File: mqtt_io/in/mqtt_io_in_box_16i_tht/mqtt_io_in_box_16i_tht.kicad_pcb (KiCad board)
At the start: 2 copper layers, 140.2 x 120.6 mm, 94 parts, among them J1 Conn_01x04_Pin, J2 Conn_01x04_Pin, U1 MCP23017_SP, U10 LTV-817, U11 LTV-817, U12 LTV-817, U13 LTV-817, U14 LTV-817, U15 LTV-817, U16 LTV-817, U17 LTV-817, U2 LTV-817, U3 LTV-817, U4 LTV-817, U5 LTV-817, U6 LTV-817, U7 LTV-817, U8 LTV-817, U9 LTV-817

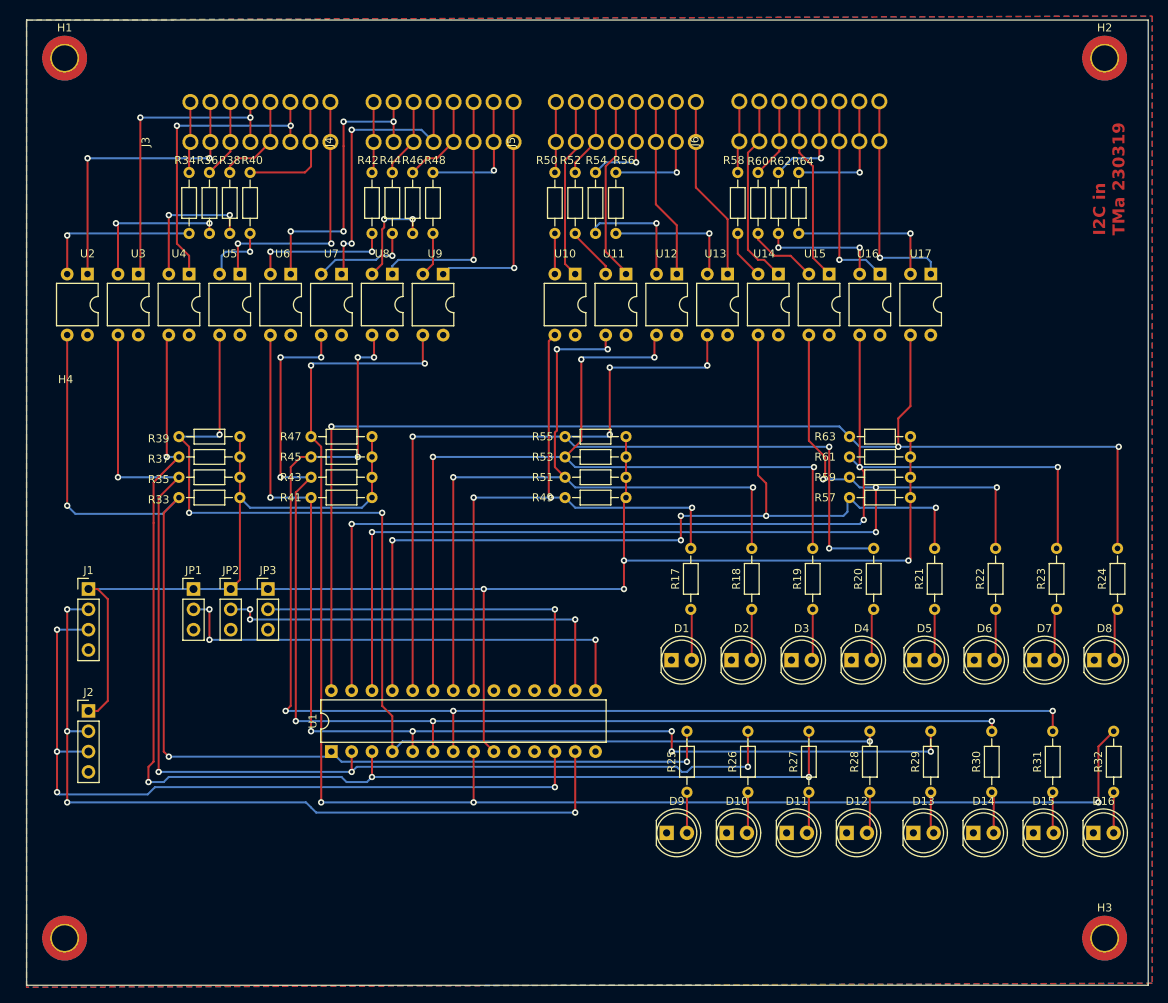
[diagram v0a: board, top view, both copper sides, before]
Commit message: Pullup für ic2 eingefügt (4k7)
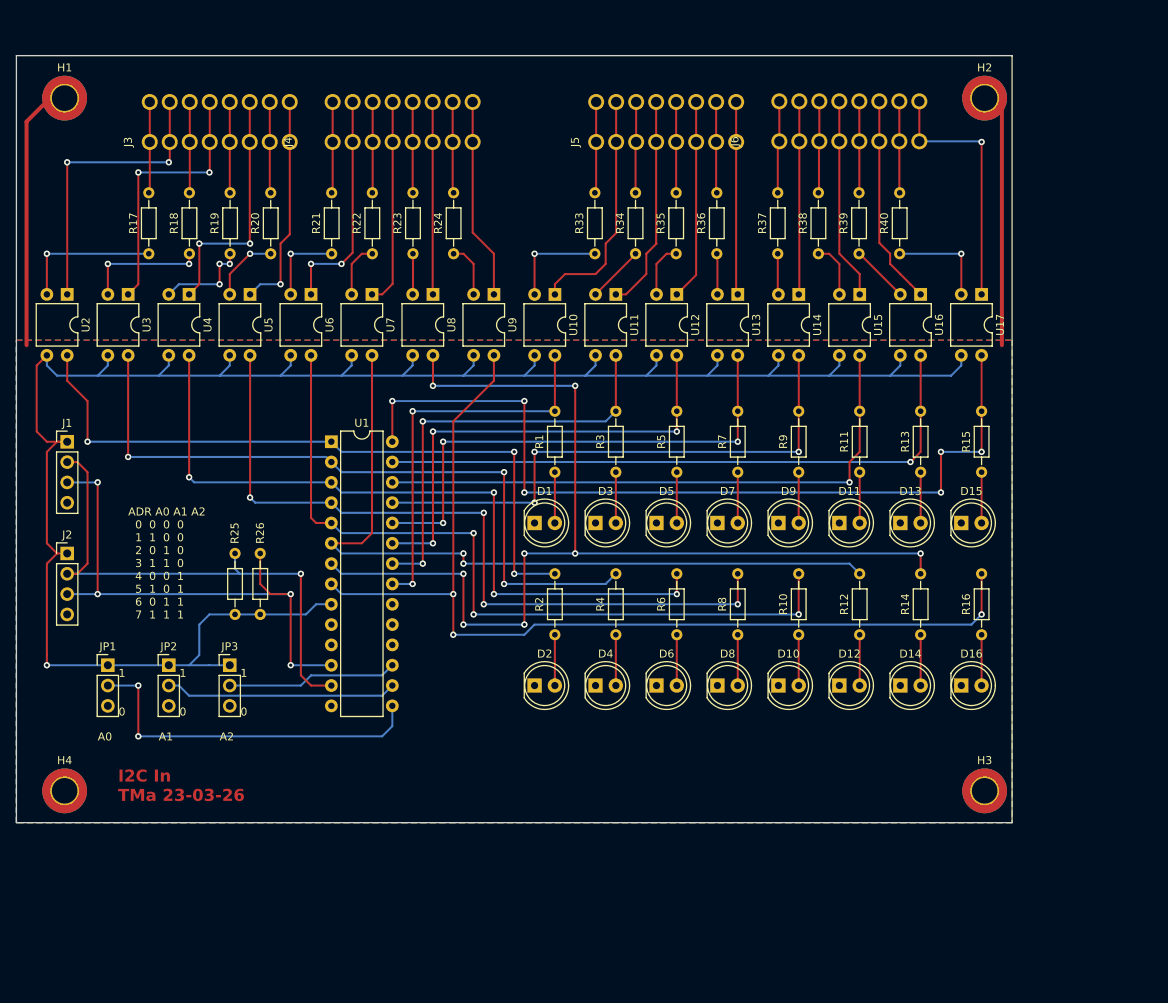
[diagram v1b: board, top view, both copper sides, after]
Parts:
- removed R27, R28, R29, R30, R31, R32: 330R, Resistor_THT:R_Axial_DIN0204_L3.6mm_D1.6mm_P7.62mm_Horizontal
- removed R41, R43, R45, R47, R49, R51, R53, R55, R57, R59, R61, R63: 10kR, Resistor_THT:R_Axial_DIN0204_L3.6mm_D1.6mm_P7.62mm_Horizontal
- removed R42, R44, R46, R48, R50, R52, R54, R56, R58, R60, R62, R64: 1200R, Resistor_THT:R_Axial_DIN0204_L3.6mm_D1.6mm_P7.62mm_Horizontal
- added R1: 330R, Resistor_THT:R_Axial_DIN0204_L3.6mm_D1.6mm_P7.62mm_Horizontal, F.Cu at (81.3, 71.8)
- added R10: 330R, Resistor_THT:R_Axial_DIN0204_L3.6mm_D1.6mm_P7.62mm_Horizontal, F.Cu at (111.8, 92.1)
- added R11: 330R, Resistor_THT:R_Axial_DIN0204_L3.6mm_D1.6mm_P7.62mm_Horizontal, F.Cu at (119.4, 71.8)
- added R12: 330R, Resistor_THT:R_Axial_DIN0204_L3.6mm_D1.6mm_P7.62mm_Horizontal, F.Cu at (119.4, 92.1)
- added R13: 330R, Resistor_THT:R_Axial_DIN0204_L3.6mm_D1.6mm_P7.62mm_Horizontal, F.Cu at (127.0, 71.8)
- added R14: 330R, Resistor_THT:R_Axial_DIN0204_L3.6mm_D1.6mm_P7.62mm_Horizontal, F.Cu at (127.0, 92.1)
- added R15: 330R, Resistor_THT:R_Axial_DIN0204_L3.6mm_D1.6mm_P7.62mm_Horizontal, F.Cu at (134.6, 71.8)
- added R16: 330R, Resistor_THT:R_Axial_DIN0204_L3.6mm_D1.6mm_P7.62mm_Horizontal, F.Cu at (134.6, 92.1)
- added R2: 330R, Resistor_THT:R_Axial_DIN0204_L3.6mm_D1.6mm_P7.62mm_Horizontal, F.Cu at (81.3, 92.1)
- added R3: 330R, Resistor_THT:R_Axial_DIN0204_L3.6mm_D1.6mm_P7.62mm_Horizontal, F.Cu at (88.9, 71.8)
- added R4: 330R, Resistor_THT:R_Axial_DIN0204_L3.6mm_D1.6mm_P7.62mm_Horizontal, F.Cu at (88.9, 92.1)
- added R5: 330R, Resistor_THT:R_Axial_DIN0204_L3.6mm_D1.6mm_P7.62mm_Horizontal, F.Cu at (96.5, 71.8)
- added R6: 330R, Resistor_THT:R_Axial_DIN0204_L3.6mm_D1.6mm_P7.62mm_Horizontal, F.Cu at (96.5, 92.1)
- added R7: 330R, Resistor_THT:R_Axial_DIN0204_L3.6mm_D1.6mm_P7.62mm_Horizontal, F.Cu at (104.1, 71.8)
- added R8: 330R, Resistor_THT:R_Axial_DIN0204_L3.6mm_D1.6mm_P7.62mm_Horizontal, F.Cu at (104.1, 92.1)
- added R9: 330R, Resistor_THT:R_Axial_DIN0204_L3.6mm_D1.6mm_P7.62mm_Horizontal, F.Cu at (111.8, 71.8)
- R17, R18, R19, R20, R21, R22, R23, R24: value 330R -> 1200R
- R25, R26: value 330R -> 4k7
- R33, R35, R37, R39: value 10kR -> 1200R
- moved R24 94.1 mm to (68.6, 44.5)
- moved R23 91.9 mm to (63.5, 44.5)
- moved R22 89.7 mm to (58.5, 44.5)
- moved R20 87.5 mm to (45.8, 44.5)
- moved R21 87.5 mm to (53.4, 44.5)
- moved R19 85.3 mm to (40.7, 44.5)
- moved R18 83.2 mm to (35.6, 44.5)
- moved R40 81.2 mm to (124.4, 44.5)
- moved R17 81.0 mm to (30.5, 44.5)
- moved R39 80.7 mm to (119.3, 44.5), turned to 90 degrees
- moved R38 73.6 mm to (114.2, 44.5)
- moved R37 71.9 mm to (109.1, 44.5), turned to 90 degrees
- moved R26 64.9 mm to (44.5, 89.5)
- moved R36 63.5 mm to (101.5, 44.5)
- moved R35 61.3 mm to (96.4, 44.5), turned to 90 degrees
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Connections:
- R17 pad 1: Net-(D1-A) -> Net-(R17-Pad1)
- R17 pad 2: /a0 -> Net-(J3-io-Pad1)
- R18 pad 1: Net-(D2-A) -> Net-(R18-Pad1)
- R18 pad 2: /a1 -> Net-(J3-io-Pad3)
- R19 pad 1: Net-(D3-A) -> Net-(R19-Pad1)
- R19 pad 2: /a2 -> Net-(J3-io-Pad5)
- R20 pad 1: Net-(D4-A) -> Net-(R20-Pad1)
- R20 pad 2: /a3 -> Net-(J3-io-Pad7)
- R21 pad 1: Net-(D5-A) -> Net-(R21-Pad1)
- R21 pad 2: /a4 -> Net-(J4-io-Pad1)
- R22 pad 1: Net-(D6-A) -> Net-(R22-Pad1)
- R22 pad 2: /a5 -> Net-(J4-io-Pad3)
- R23 pad 1: Net-(D7-A) -> Net-(R23-Pad1)
- R23 pad 2: /a6 -> Net-(J4-io-Pad5)
- R24 pad 1: Net-(D8-A) -> Net-(R24-Pad1)
- R24 pad 2: /a7 -> Net-(J4-io-Pad7)
- R25 pad 1: Net-(D9-A) -> +5V
- R25 pad 2: /b0 -> Net-(J1-Pin_2)
- R26 pad 1: Net-(D10-A) -> +5V
- R26 pad 2: /b1 -> Net-(J1-Pin_3)
- R33 pad 1: +5V -> Net-(R33-Pad1)
- R33 pad 2: /b0 -> Net-(J5-io-Pad1)
- R34 pad 2: Net-(J3-io-Pad1) -> Net-(J5-io-Pad3)
- R35 pad 1: +5V -> Net-(R35-Pad1)
- R35 pad 2: /b1 -> Net-(J5-io-Pad5)
- R36 pad 2: Net-(J3-io-Pad3) -> Net-(J5-io-Pad7)
- R37 pad 1: +5V -> Net-(R37-Pad1)
- R37 pad 2: /b2 -> Net-(J6-io-Pad1)
- R38 pad 2: Net-(J3-io-Pad5) -> Net-(J6-io-Pad3)
- R39 pad 1: +5V -> Net-(R39-Pad1)
- R39 pad 2: /b3 -> Net-(J6-io-Pad5)
- R40 pad 2: Net-(J3-io-Pad7) -> Net-(J6-io-Pad7)
- U10 pad 2: Net-(R50-Pad1) -> Net-(R33-Pad1)
- U10 pad 3: /a0 -> +5V
- U10 pad 4: GND -> /a0
- U11 pad 2: Net-(R52-Pad1) -> Net-(R34-Pad1)
- U11 pad 3: /a1 -> +5V
- U11 pad 4: GND -> /a1
- U12 pad 2: Net-(R54-Pad1) -> Net-(R35-Pad1)
- U12 pad 3: /a2 -> +5V
- U12 pad 4: GND -> /a2
- U13 pad 2: Net-(R56-Pad1) -> Net-(R36-Pad1)
- U13 pad 3: /a3 -> +5V
- U13 pad 4: GND -> /a3
- U14 pad 2: Net-(R58-Pad1) -> Net-(R37-Pad1)
- U14 pad 3: /a4 -> +5V
- U14 pad 4: GND -> /a4
- U15 pad 2: Net-(R60-Pad1) -> Net-(R38-Pad1)
- U15 pad 3: /a5 -> +5V
- U15 pad 4: GND -> /a5
- U16 pad 2: Net-(R62-Pad1) -> Net-(R39-Pad1)
- U16 pad 3: /a6 -> +5V
- U16 pad 4: GND -> /a6
- U17 pad 2: Net-(R64-Pad1) -> Net-(R40-Pad1)
- U17 pad 3: /a7 -> +5V
- U17 pad 4: GND -> /a7
- U2 pad 2: Net-(R34-Pad1) -> Net-(R17-Pad1)
- U2 pad 3: /b0 -> +5V
- U2 pad 4: GND -> /b0
- U3 pad 2: Net-(R36-Pad1) -> Net-(R18-Pad1)
- U3 pad 3: /b1 -> +5V
- U3 pad 4: GND -> /b1
- U4 pad 2: Net-(R38-Pad1) -> Net-(R19-Pad1)
- U4 pad 3: /b2 -> +5V
- U4 pad 4: GND -> /b2
- U5 pad 2: Net-(R40-Pad1) -> Net-(R20-Pad1)
- U5 pad 3: /b3 -> +5V
- U5 pad 4: GND -> /b3
- U6 pad 2: Net-(R42-Pad1) -> Net-(R21-Pad1)
- U6 pad 3: /b4 -> +5V
- U6 pad 4: GND -> /b4
- U7 pad 2: Net-(R44-Pad1) -> Net-(R22-Pad1)
- U7 pad 3: /b5 -> +5V
- U7 pad 4: GND -> /b5
- U8 pad 2: Net-(R46-Pad1) -> Net-(R23-Pad1)
- U8 pad 3: /b6 -> +5V
- U8 pad 4: GND -> /b6
- U9 pad 2: Net-(R48-Pad1) -> Net-(R24-Pad1)
- U9 pad 3: /b7 -> +5V
- U9 pad 4: GND -> /b7
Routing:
- net /a3: track 132.8 -> 64.1 mm, vias 6 -> 3
- net GND: track 0.00 -> 66.7 mm
- net /a6: track 145.2 -> 78.6 mm, vias 4 -> 1
- net /a5: track 137.4 -> 73.5 mm, vias 5 -> 1
- net /b7: track 186.3 -> 125.0 mm, vias 5 -> 3
- net /b2: track 151.3 -> 92.2 mm
- net /b1: track 144.7 -> 88.9 mm, vias 4 -> 3
- net /b5: track 150.0 -> 96.2 mm, vias 6 -> 2
- net /a2: track 112.8 -> 59.1 mm, vias 4 -> 3
- net /b0: track 139.4 -> 86.0 mm
- net /a7: track 159.9 -> 107.3 mm, vias 3 -> 6
- net /a4: track 120.3 -> 69.2 mm, vias 5 -> 3
- net /b3: track 143.7 -> 94.8 mm
- net /a1: track 97.2 -> 53.2 mm, vias 4 -> 2
- net /b4: track 139.7 -> 97.3 mm, vias 6 -> 3
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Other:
- board size 140.2 x 120.6 mm -> 124.5 x 95.9 mm
- board text added: "1 0"
- board text added: "A0"
- board text added: "A1"
- board text added: "A2"
- board text added: "ADR A0 A1 A2 0 0 0 0 1 1 0 0 2 0 1 0 3 1 1 0 4 0 0 1 5 1 0 1 6 0 1 1 7 1 1 1"
- board text added: "I2C In TMa 23-03-26"
- board text removed: "I2C in TMa 230319"

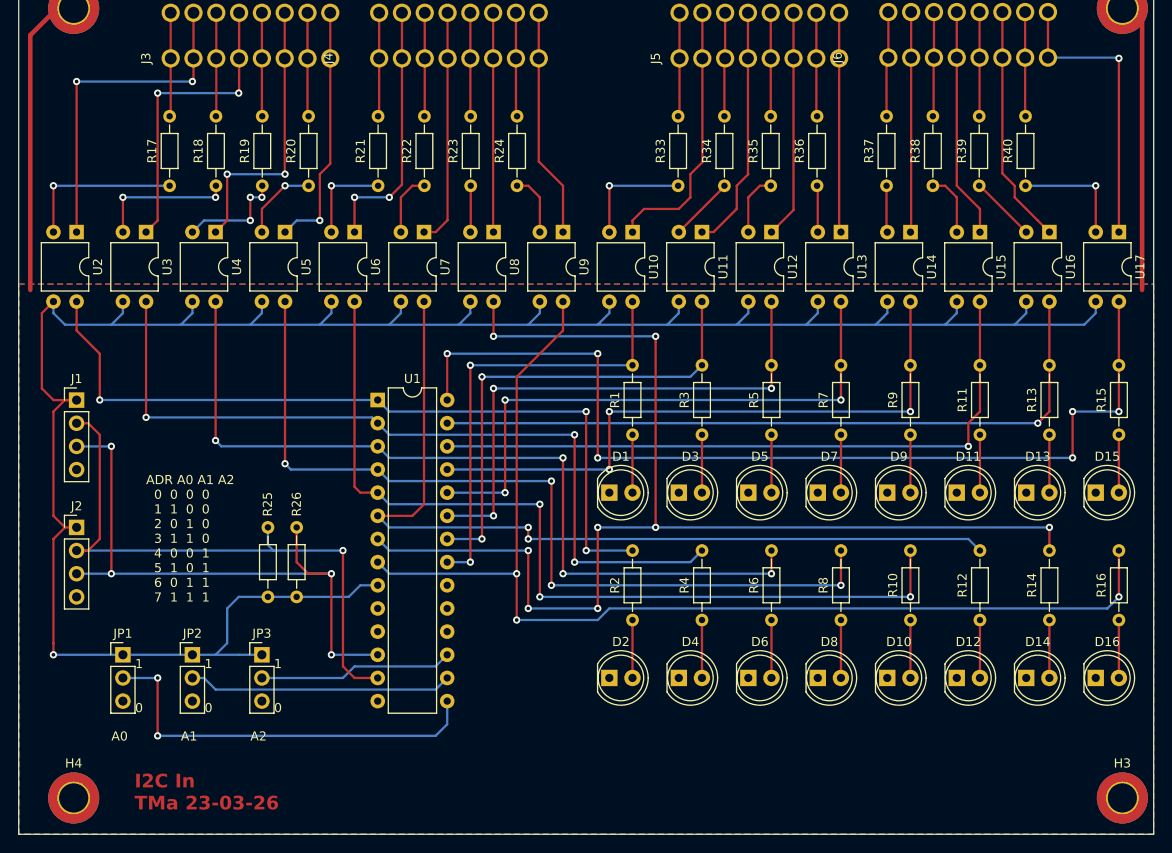
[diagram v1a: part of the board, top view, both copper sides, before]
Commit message: neue Dateien eingefügt.
out Platine rev 2, testprogramm für pi pico
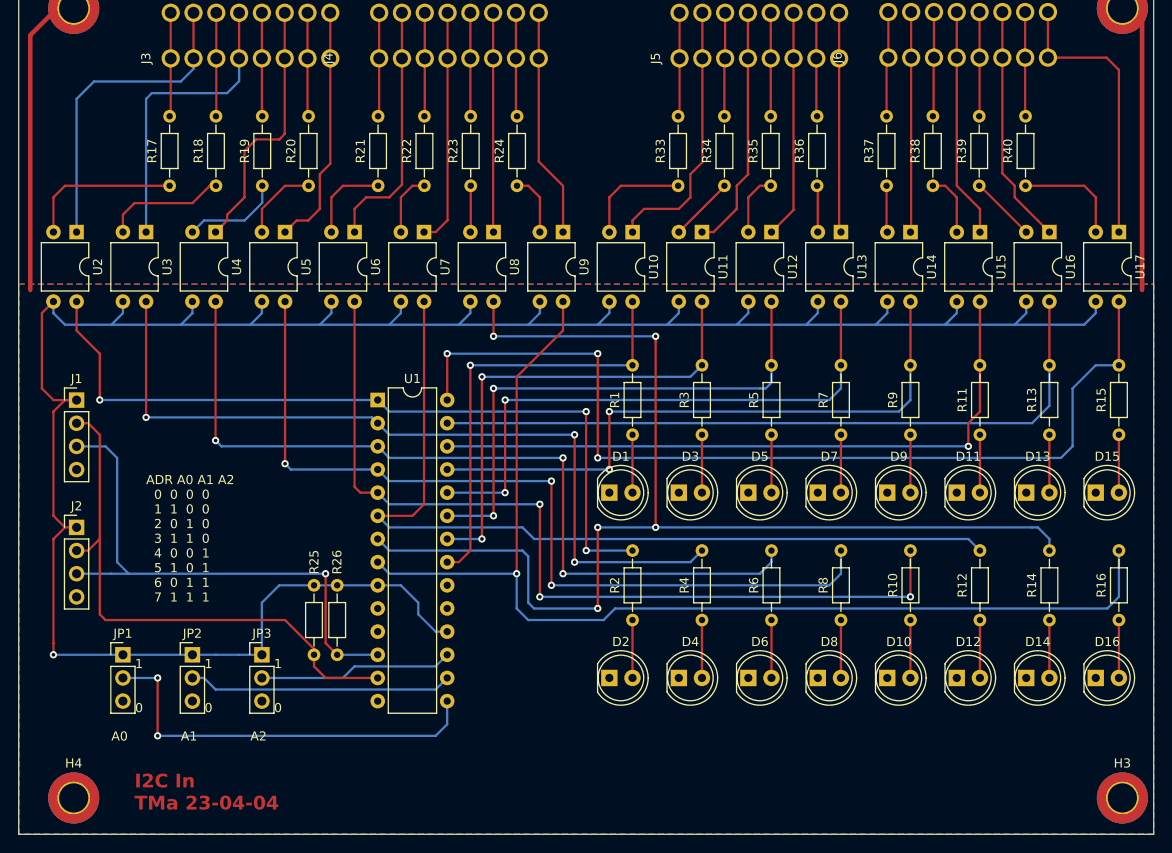
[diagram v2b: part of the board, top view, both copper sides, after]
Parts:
- moved R25 5.21 mm to (46.4, 88.3), turned to -90 degrees
- moved R26 4.62 mm to (48.9, 88.3), turned to -90 degrees
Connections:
- J1 pad 1: +5V -> VDD
- J2 pad 1: +5V -> VDD
- JP1 pad 1: +5V -> VDD
- JP2 pad 1: +5V -> VDD
- JP3 pad 1: +5V -> VDD
- R25 pad 1: +5V -> VDD
- R26 pad 1: +5V -> VDD
- U1 pad 18: GND -> VDD
- U1 pad 9: +5V -> VDD
- U10 pad 3: +5V -> VDD
- U11 pad 3: +5V -> VDD
- U12 pad 3: +5V -> VDD
- U13 pad 3: +5V -> VDD
- U14 pad 3: +5V -> VDD
- U15 pad 3: +5V -> VDD
- U16 pad 3: +5V -> VDD
- U17 pad 3: +5V -> VDD
- U2 pad 3: +5V -> VDD
- U3 pad 3: +5V -> VDD
- U4 pad 3: +5V -> VDD
- U5 pad 3: +5V -> VDD
- U6 pad 3: +5V -> VDD
- U7 pad 3: +5V -> VDD
- U8 pad 3: +5V -> VDD
- U9 pad 3: +5V -> VDD
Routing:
- net VDD: track 0.00 -> 259.8 mm, vias 0 -> 1
- net +5V: track 253.3 -> 0.00 mm, vias 1 -> 0
- net Net-(J1-Pin_3): track 67.8 -> 59.4 mm, vias 4 -> 1
- net Net-(J1-Pin_2): track 66.6 -> 60.3 mm, vias 1 -> 0
- net Net-(J3-io-Pad6): track 30.9 -> 28.7 mm, vias 2 -> 0
- net /a7: track 107.3 -> 105.1 mm, vias 6 -> 3
- net Net-(J3-io-Pad2): track 36.8 -> 34.9 mm, vias 2 -> 0
- net Net-(R18-Pad1): track 15.3 -> 13.4 mm, vias 2 -> 0
- net /b6: track 134.5 -> 133.0 mm, vias 8 -> 5
- net Net-(R19-Pad1): track 12.0 -> 10.9 mm, vias 3 -> 0
- net /b7: track 125.0 -> 124.2 mm, vias 3 -> 1
- net /b2: track 92.2 -> 91.5 mm, vias 4 -> 3
- net /a4: track 69.2 -> 68.5 mm, vias 3 -> 2
- net Net-(J4-io-Pad2): track 28.4 -> 27.7 mm, vias 2 -> 0
- net /a0: track 48.9 -> 48.1 mm, vias 2 -> 1
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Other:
- board text added: "I2C In TMa 23-04-04"
- board text removed: "I2C In TMa 23-03-26"

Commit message: Add files via upload
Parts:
- removed JP1, JP2, JP3: Jumper_3_Open, Connector_PinHeader_2.54mm:PinHeader_1x03_P2.54mm_Vertical
- added D17: 5,1V, Diode_THT:D_DO-41_SOD81_P10.16mm_Horizontal, F.Cu at (-85.7, 53.7)
- added D18: 5,1V, Diode_THT:D_DO-41_SOD81_P10.16mm_Horizontal, F.Cu at (-85.7, 58.0)
- added D19: 5,1V, Diode_THT:D_DO-41_SOD81_P10.16mm_Horizontal, F.Cu at (-85.7, 62.2)
- added D20: 5,1V, Diode_THT:D_DO-41_SOD81_P10.16mm_Horizontal, F.Cu at (-85.7, 66.5)
- added D21: 5,1V, Diode_THT:D_DO-41_SOD81_P10.16mm_Horizontal, F.Cu at (-85.7, 70.7)
- added D22: 5,1V, Diode_THT:D_DO-41_SOD81_P10.16mm_Horizontal, F.Cu at (-85.7, 75.0)
- added D23: 5,1V, Diode_THT:D_DO-41_SOD81_P10.16mm_Horizontal, F.Cu at (-85.7, 79.2)
- added D24: 5,1V, Diode_THT:D_DO-41_SOD81_P10.16mm_Horizontal, F.Cu at (-85.7, 83.5)
- added D25: LED, Diode_THT:D_DO-41_SOD81_P10.16mm_Horizontal, F.Cu at (-85.7, 87.7)
- added D26: LED, Diode_THT:D_DO-41_SOD81_P10.16mm_Horizontal, F.Cu at (-85.7, 92.0)
- added D27: LED, Diode_THT:D_DO-41_SOD81_P10.16mm_Horizontal, F.Cu at (-85.7, 96.2)
- added D28: LED, Diode_THT:D_DO-41_SOD81_P10.16mm_Horizontal, F.Cu at (-85.7, 100.5)
- added D29: LED, Diode_THT:D_DO-41_SOD81_P10.16mm_Horizontal, F.Cu at (-85.7, 104.7)
- added D30: LED, Diode_THT:D_DO-41_SOD81_P10.16mm_Horizontal, F.Cu at (-85.7, 109.0)
- added D31: LED, Diode_THT:D_DO-41_SOD81_P10.16mm_Horizontal, F.Cu at (-85.7, 113.2)
- added D32: LED, Diode_THT:D_DO-41_SOD81_P10.16mm_Horizontal, F.Cu at (-85.7, 117.5)
- added J10: Sig_in_1, parts_tma_1:AST_041-2, F.Cu at (66.7, 33.7)
- added J11: Sig_in_1, parts_tma_1:AST_041-2, F.Cu at (73.0, 33.7)
- added J12: Sig_in_1, parts_tma_1:AST_041-2, F.Cu at (79.4, 33.7)
- added J13: Sig_in_1, parts_tma_1:AST_041-2, F.Cu at (85.7, 33.7)
- added J14: Sig_in_1, parts_tma_1:AST_041-2, F.Cu at (92.1, 33.7)
- added J15: Sig_in_1, parts_tma_1:AST_041-2, F.Cu at (98.4, 33.7)
- added J16: Sig_in_1, parts_tma_1:AST_041-2, F.Cu at (104.8, 33.7)
- added J17: Sig_in_1, parts_tma_1:AST_041-2, F.Cu at (111.1, 33.7)
- added J18: Sig_in_1, parts_tma_1:AST_041-2, F.Cu at (117.5, 33.7)
- added J19: Sig_in_1, parts_tma_1:AST_041-2, F.Cu at (123.8, 33.7)
- added J7: Sig_in_1, parts_tma_1:AST_041-2, F.Cu at (47.6, 33.7)
- added J8: Sig_in_1, parts_tma_1:AST_041-2, F.Cu at (54.0, 33.7)
- added J9: Sig_in_1, parts_tma_1:AST_041-2, F.Cu at (60.3, 33.7)
- added R27: 82R, Resistor_THT:R_Axial_DIN0204_L3.6mm_D1.6mm_P7.62mm_Horizontal, F.Cu at (-72.2, 53.2)
- added R28: 82R, Resistor_THT:R_Axial_DIN0204_L3.6mm_D1.6mm_P7.62mm_Horizontal, F.Cu at (-72.2, 56.3)
- added R29: 10k, Resistor_THT:R_Axial_DIN0204_L3.6mm_D1.6mm_P7.62mm_Horizontal, F.Cu at (-72.2, 59.5)
- added R30: 10k, Resistor_THT:R_Axial_DIN0204_L3.6mm_D1.6mm_P7.62mm_Horizontal, F.Cu at (-72.2, 62.6)
- added R31: 10k, Resistor_THT:R_Axial_DIN0204_L3.6mm_D1.6mm_P7.62mm_Horizontal, F.Cu at (-72.2, 65.8)
- added R32: 10k, Resistor_THT:R_Axial_DIN0204_L3.6mm_D1.6mm_P7.62mm_Horizontal, F.Cu at (-72.2, 68.9)
- added R41: R, Resistor_THT:R_Axial_DIN0204_L3.6mm_D1.6mm_P7.62mm_Horizontal, F.Cu at (-72.2, 72.1)
- added R42: R, Resistor_THT:R_Axial_DIN0204_L3.6mm_D1.6mm_P7.62mm_Horizontal, F.Cu at (-72.2, 75.2)
- added R43: R, Resistor_THT:R_Axial_DIN0204_L3.6mm_D1.6mm_P7.62mm_Horizontal, F.Cu at (-72.2, 78.4)
- added R44: R, Resistor_THT:R_Axial_DIN0204_L3.6mm_D1.6mm_P7.62mm_Horizontal, F.Cu at (-72.2, 81.5)
- added R45: 680R, Resistor_THT:R_Axial_DIN0204_L3.6mm_D1.6mm_P7.62mm_Horizontal, F.Cu at (-72.2, 84.7)
- added R46: 680R, Resistor_THT:R_Axial_DIN0204_L3.6mm_D1.6mm_P7.62mm_Horizontal, F.Cu at (-72.2, 87.8)
- added R47: 680R, Resistor_THT:R_Axial_DIN0204_L3.6mm_D1.6mm_P7.62mm_Horizontal, F.Cu at (-61.6, 53.2)
- added R48: 680R, Resistor_THT:R_Axial_DIN0204_L3.6mm_D1.6mm_P7.62mm_Horizontal, F.Cu at (-61.6, 56.3)
- added R49: 680R, Resistor_THT:R_Axial_DIN0204_L3.6mm_D1.6mm_P7.62mm_Horizontal, F.Cu at (-61.6, 59.5)
- added R50: 680R, Resistor_THT:R_Axial_DIN0204_L3.6mm_D1.6mm_P7.62mm_Horizontal, F.Cu at (-61.6, 62.6)
- added R51: 680R, Resistor_THT:R_Axial_DIN0204_L3.6mm_D1.6mm_P7.62mm_Horizontal, F.Cu at (-61.6, 65.8)
- added R52: 680R, Resistor_THT:R_Axial_DIN0204_L3.6mm_D1.6mm_P7.62mm_Horizontal, F.Cu at (-61.6, 68.9)
- added R53: 82R, Resistor_THT:R_Axial_DIN0204_L3.6mm_D1.6mm_P7.62mm_Horizontal, F.Cu at (-61.6, 72.1)
- added R54: 82R, Resistor_THT:R_Axial_DIN0204_L3.6mm_D1.6mm_P7.62mm_Horizontal, F.Cu at (-61.6, 75.2)
- added R55: 82R, Resistor_THT:R_Axial_DIN0204_L3.6mm_D1.6mm_P7.62mm_Horizontal, F.Cu at (-61.6, 78.4)
- added R56: 82R, Resistor_THT:R_Axial_DIN0204_L3.6mm_D1.6mm_P7.62mm_Horizontal, F.Cu at (-61.6, 81.5)
- added R57: 82R, Resistor_THT:R_Axial_DIN0204_L3.6mm_D1.6mm_P7.62mm_Horizontal, F.Cu at (-61.6, 84.7)
- added R58: 82R, Resistor_THT:R_Axial_DIN0204_L3.6mm_D1.6mm_P7.62mm_Horizontal, F.Cu at (-61.6, 87.8)
- added R59: 82R, Resistor_THT:R_Axial_DIN0204_L3.6mm_D1.6mm_P7.62mm_Horizontal, F.Cu at (-51.1, 53.2)
- added R60: 82R, Resistor_THT:R_Axial_DIN0204_L3.6mm_D1.6mm_P7.62mm_Horizontal, F.Cu at (-51.1, 56.3)
- added R61: 10k, Resistor_THT:R_Axial_DIN0204_L3.6mm_D1.6mm_P7.62mm_Horizontal, F.Cu at (-51.1, 59.5)
- added R62: 10k, Resistor_THT:R_Axial_DIN0204_L3.6mm_D1.6mm_P7.62mm_Horizontal, F.Cu at (-51.1, 62.6)
- added R63: 10k, Resistor_THT:R_Axial_DIN0204_L3.6mm_D1.6mm_P7.62mm_Horizontal, F.Cu at (-51.1, 65.8)
- added R64: 10k, Resistor_THT:R_Axial_DIN0204_L3.6mm_D1.6mm_P7.62mm_Horizontal, F.Cu at (-51.1, 68.9)
- added R65: 10k, Resistor_THT:R_Axial_DIN0204_L3.6mm_D1.6mm_P7.62mm_Horizontal, F.Cu at (-51.1, 72.1)
- added R66: 10k, Resistor_THT:R_Axial_DIN0204_L3.6mm_D1.6mm_P7.62mm_Horizontal, F.Cu at (-51.1, 75.2)
- added R67: 10k, Resistor_THT:R_Axial_DIN0204_L3.6mm_D1.6mm_P7.62mm_Horizontal, F.Cu at (-51.1, 78.4)
- added R68: 10k, Resistor_THT:R_Axial_DIN0204_L3.6mm_D1.6mm_P7.62mm_Horizontal, F.Cu at (-51.1, 81.5)
- added SW1: SW_DIP_x03, Package_DIP:DIP-6_W7.62mm_LongPads, F.Cu at (-71.7, 91.5)
- D1, D2, D3, D4, D5, D6, D7, D8: value LED -> 5,1V; footprint LED_THT:LED_D5.0mm -> Diode_THT:D_DO-41_SOD81_P10.16mm_Horizontal
- J1: value Conn_01x04_Pin -> SPI THROUGH; footprint Connector_PinHeader_2.54mm:PinHeader_1x04_P2.54mm_Vertical -> Connector_PinHeader_2.54mm:PinHeader_1x05_P2.54mm_Vertical
- J2: value Conn_01x04_Pin -> SPI IN; footprint Connector_PinHeader_2.54mm:PinHeader_1x04_P2.54mm_Vertical -> Connector_PinHeader_2.54mm:PinHeader_1x05_P2.54mm_Vertical
- J3: value ~ -> PWR; footprint parts_tma_1:AST041-08 -> parts_tma_1:AST_041-2
- J4, J5, J6: value ~ -> Sig_in_1; footprint parts_tma_1:AST041-08 -> parts_tma_1:AST_041-2
- R1, R3, R4: value 330R -> 3k3
- R10, R11, R12, R5, R6, R7, R8, R9: value 330R -> R
- R13, R14, R15, R16: value 330R -> 680R
- R17, R18, R19, R20: value 1200R -> 680R
- R2: value 330R -> 10k
- R21, R22, R23, R24: value 1200R -> 82R
- R25, R26: value 4k7 -> 82R
- R33, R34, R35, R36: value 1200R -> 10k
- R37, R38, R39, R40: value 1200R -> R
- U1: value MCP23017_SP -> MCP23S17_SP
- moved D15 286.8 mm to (-153.9, 99.2)
- moved D13 278.7 mm to (-153.9, 91.6)
- moved D16 278.5 mm to (-146.4, 99.2)
- moved D14 271.0 mm to (-146.4, 91.6)
- moved D11 270.8 mm to (-153.9, 84.1)
- moved D12 263.7 mm to (-146.4, 84.1)
- moved D10 256.6 mm to (-146.4, 76.5)
- moved R16 251.2 mm to (-111.8, 43.6), turned to 0 degrees
- moved R15 248.4 mm to (-111.8, 40.4), turned to 0 degrees
- moved R14 245.0 mm to (-111.8, 37.3), turned to 0 degrees
- moved R12 242.9 mm to (-122.4, 68.8), turned to 0 degrees
- moved R11 241.8 mm to (-122.4, 65.6), turned to 0 degrees
- moved R10 236.0 mm to (-122.4, 62.5), turned to 0 degrees
- moved R9 234.5 mm to (-122.4, 59.3), turned to 0 degrees
- moved R8 229.3 mm to (-122.4, 56.2), turned to 0 degrees
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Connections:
- D1 pad 1: GND -> Net-(D1-K)
- D10 pad 1: GND -> Net-(D10-K)
- D11 pad 1: GND -> Net-(D11-K)
- D12 pad 1: GND -> Net-(D12-K)
- D13 pad 1: GND -> Net-(D13-K)
- D14 pad 1: GND -> Net-(D14-K)
- D15 pad 1: GND -> Net-(D15-K)
- D16 pad 1: GND -> Net-(D16-K)
- D2 pad 1: GND -> Net-(D2-K)
- D2 pad 2: Net-(D2-A) -> Net-(D10-K)
- D3 pad 1: GND -> Net-(D3-K)
- D3 pad 2: Net-(D3-A) -> Net-(D11-K)
- D4 pad 1: GND -> Net-(D4-K)
- D4 pad 2: Net-(D4-A) -> Net-(D12-K)
- D5 pad 1: GND -> Net-(D5-K)
- D5 pad 2: Net-(D5-A) -> Net-(D13-K)
- D6 pad 1: GND -> Net-(D6-K)
- D6 pad 2: Net-(D6-A) -> Net-(D14-K)
- D7 pad 1: GND -> Net-(D7-K)
- D7 pad 2: Net-(D7-A) -> Net-(D15-K)
- D8 pad 1: GND -> Net-(D8-K)
- D8 pad 2: Net-(D8-A) -> Net-(D16-K)
- D9 pad 1: GND -> Net-(D1-A)
- J1 pad 1: VDD -> Net-(J1-Pin_1)
- J1 pad 4: GND -> Net-(J1-Pin_4)
- J2 pad 1: VDD -> Net-(J1-Pin_1)
- J2 pad 4: GND -> Net-(J1-Pin_4)
- J3 pad 1: Net-(J3-io-Pad1) -> VDD
- J3 pad 2: Net-(J3-io-Pad2) -> GND
- J4 pad 1: Net-(J4-io-Pad1) -> Net-(J4-Pad1)
- J4 pad 2: Net-(J4-io-Pad2) -> Net-(D1-A)
- J5 pad 1: Net-(J5-io-Pad1) -> Net-(J5-Pad1)
- J5 pad 2: Net-(J5-io-Pad2) -> Net-(D10-K)
- J6 pad 1: Net-(J6-io-Pad1) -> Net-(J6-Pad1)
- J6 pad 2: Net-(J6-io-Pad2) -> Net-(D11-K)
- R1 pad 1: Net-(D1-A) -> Net-(U1-A0)
- R1 pad 2: /a0 -> GND
- R10 pad 1: Net-(D10-A) -> Net-(J8-Pad1)
- R10 pad 2: /b4 -> Net-(D6-K)
- R11 pad 1: Net-(D11-A) -> Net-(J9-Pad1)
- R11 pad 2: /a5 -> Net-(D7-K)
- R12 pad 1: Net-(D12-A) -> Net-(J10-Pad1)
- R12 pad 2: /b5 -> Net-(D8-K)
- R13 pad 1: Net-(D13-A) -> Net-(D1-K)
- R13 pad 2: /a6 -> Net-(D9-A)
- R14 pad 1: Net-(D14-A) -> Net-(D2-K)
- R14 pad 2: /b6 -> Net-(D10-A)
- R15 pad 1: Net-(D15-A) -> Net-(D3-K)
- R15 pad 2: /a7 -> Net-(D11-A)
- R16 pad 1: Net-(D16-A) -> Net-(D4-K)
- R16 pad 2: /b7 -> Net-(D12-A)
- R17 pad 1: Net-(R17-Pad1) -> Net-(D5-K)
- R17 pad 2: Net-(J3-io-Pad1) -> Net-(D13-A)
- R18 pad 1: Net-(R18-Pad1) -> Net-(D6-K)
- R18 pad 2: Net-(J3-io-Pad3) -> Net-(D14-A)
- R19 pad 1: Net-(R19-Pad1) -> Net-(D7-K)
- R19 pad 2: Net-(J3-io-Pad5) -> Net-(D15-A)
- R2 pad 1: Net-(D2-A) -> VDD
- R2 pad 2: /b0 -> Net-(U1-~{RESET})
- R20 pad 1: Net-(R20-Pad1) -> Net-(D8-K)
- R20 pad 2: Net-(J3-io-Pad7) -> Net-(D16-A)
- R21 pad 1: Net-(R21-Pad1) -> Net-(D1-K)
- R21 pad 2: Net-(J4-io-Pad1) -> Net-(R21-Pad2)
- R22 pad 1: Net-(R22-Pad1) -> Net-(D2-K)
- R22 pad 2: Net-(J4-io-Pad3) -> Net-(R22-Pad2)
- R23 pad 1: Net-(R23-Pad1) -> Net-(D3-K)
- R23 pad 2: Net-(J4-io-Pad5) -> Net-(R23-Pad2)
- R24 pad 1: Net-(R24-Pad1) -> Net-(D4-K)
- R24 pad 2: Net-(J4-io-Pad7) -> Net-(R24-Pad2)
- R25 pad 1: VDD -> Net-(D5-K)
- R25 pad 2: Net-(J1-Pin_2) -> Net-(R25-Pad2)
- R26 pad 1: VDD -> Net-(D6-K)
- R26 pad 2: Net-(J1-Pin_3) -> Net-(R26-Pad2)
- R3 pad 1: Net-(D3-A) -> Net-(U1-A1)
- R3 pad 2: /a1 -> GND
- R33 pad 1: Net-(R33-Pad1) -> /IN_1_5
- R33 pad 2: Net-(J5-io-Pad1) -> GND
- R34 pad 1: Net-(R34-Pad1) -> /IN_1_6
- R34 pad 2: Net-(J5-io-Pad3) -> GND
- R35 pad 1: Net-(R35-Pad1) -> /IN_1_7
- R35 pad 2: Net-(J5-io-Pad5) -> GND
- R36 pad 1: Net-(R36-Pad1) -> /IN_1_8
- R36 pad 2: Net-(J5-io-Pad7) -> GND
- R37 pad 1: Net-(R37-Pad1) -> Net-(J12-Pad1)
- R37 pad 2: Net-(J6-io-Pad1) -> Net-(D17-K)
- R38 pad 1: Net-(R38-Pad1) -> Net-(J13-Pad1)
- R38 pad 2: Net-(J6-io-Pad3) -> Net-(D18-K)
- R39 pad 1: Net-(R39-Pad1) -> Net-(J14-Pad1)
- R39 pad 2: Net-(J6-io-Pad5) -> Net-(D19-K)
- R4 pad 1: Net-(D4-A) -> Net-(U1-A2)
- R4 pad 2: /b1 -> GND
- R40 pad 1: Net-(R40-Pad1) -> Net-(J15-Pad1)
- R40 pad 2: Net-(J6-io-Pad7) -> Net-(D20-K)
- R5 pad 1: Net-(D5-A) -> Net-(J4-Pad1)
- R5 pad 2: /a2 -> Net-(D1-K)
- R6 pad 1: Net-(D6-A) -> Net-(J5-Pad1)
- R6 pad 2: /b2 -> Net-(D2-K)
- R7 pad 1: Net-(D7-A) -> Net-(J6-Pad1)
- R7 pad 2: /a3 -> Net-(D3-K)
- R8 pad 1: Net-(D8-A) -> Net-(J7-Pad1)
- R8 pad 2: /b3 -> Net-(D4-K)
- R9 pad 1: Net-(D9-A) -> Net-(J11-Pad1)
- R9 pad 2: /a4 -> Net-(D5-K)
- U1 pad 1: /b0 -> /IN_2_1
- U1 pad 11: unconnected-(U1-NC-Pad11) -> Net-(J1-Pin_1)
- U1 pad 12: Net-(J1-Pin_3) -> Net-(J1-Pin_2)
- U1 pad 13: Net-(J1-Pin_2) -> Net-(J1-Pin_3)
- U1 pad 14: unconnected-(U1-NC-Pad14) -> Net-(J1-Pin_4)
- U1 pad 15: /AD0 -> Net-(U1-A0)
- U1 pad 16: /AD1 -> Net-(U1-A1)
- U1 pad 17: /AD2 -> Net-(U1-A2)
- U1 pad 18: VDD -> Net-(U1-~{RESET})
- U1 pad 2: /b1 -> /IN_2_2
- U1 pad 21: /a0 -> /IN_1_1
- U1 pad 22: /a1 -> /IN_1_2
- U1 pad 23: /a2 -> /IN_1_3
- U1 pad 24: /a3 -> /IN_1_4
- U1 pad 25: /a4 -> /IN_1_5
- U1 pad 26: /a5 -> /IN_1_6
- U1 pad 27: /a6 -> /IN_1_7
- U1 pad 28: /a7 -> /IN_1_8
- U1 pad 3: /b2 -> /IN_2_3
- U1 pad 4: /b3 -> /IN_2_4
- U1 pad 5: /b4 -> /IN_2_5
- U1 pad 6: /b5 -> /IN_2_6
- U1 pad 7: /b6 -> /IN_2_7
- U1 pad 8: /b7 -> /IN_2_8
- U10 pad 1: Net-(J5-io-Pad2) -> Net-(R53-Pad2)
- U10 pad 2: Net-(R33-Pad1) -> Net-(D17-A)
- U10 pad 3: VDD -> /IN_2_1
- U10 pad 4: /a0 -> VDD
- U11 pad 1: Net-(J5-io-Pad4) -> Net-(R54-Pad2)
- U11 pad 2: Net-(R34-Pad1) -> Net-(D18-A)
- U11 pad 3: VDD -> /IN_2_2
- U11 pad 4: /a1 -> VDD
- U12 pad 1: Net-(J5-io-Pad6) -> Net-(R55-Pad2)
- U12 pad 2: Net-(R35-Pad1) -> Net-(D19-A)
- U12 pad 3: VDD -> /IN_2_3
- U12 pad 4: /a2 -> VDD
- U13 pad 1: Net-(J5-io-Pad8) -> Net-(R56-Pad2)
- U13 pad 2: Net-(R36-Pad1) -> Net-(D20-A)
- U13 pad 3: VDD -> /IN_2_4
- U13 pad 4: /a3 -> VDD
- U14 pad 1: Net-(J6-io-Pad2) -> Net-(R57-Pad2)
- U14 pad 2: Net-(R37-Pad1) -> Net-(D21-A)
- U14 pad 3: VDD -> /IN_2_5
- U14 pad 4: /a4 -> VDD
- U15 pad 1: Net-(J6-io-Pad4) -> Net-(R58-Pad2)
- U15 pad 2: Net-(R38-Pad1) -> Net-(D22-A)
- U15 pad 3: VDD -> /IN_2_6
- U15 pad 4: /a5 -> VDD
- U16 pad 1: Net-(J6-io-Pad6) -> Net-(R59-Pad2)
- U16 pad 2: Net-(R39-Pad1) -> Net-(D23-A)
- U16 pad 3: VDD -> /IN_2_7
- U16 pad 4: /a6 -> VDD
- U17 pad 1: Net-(J6-io-Pad8) -> Net-(R60-Pad2)
- U17 pad 2: Net-(R40-Pad1) -> Net-(D24-A)
- U17 pad 3: VDD -> /IN_2_8
- U17 pad 4: /a7 -> VDD
- U2 pad 1: Net-(J3-io-Pad2) -> Net-(R21-Pad2)
- U2 pad 2: Net-(R17-Pad1) -> Net-(D1-A)
- U2 pad 3: VDD -> /IN_1_1
- U2 pad 4: /b0 -> VDD
- U3 pad 1: Net-(J3-io-Pad4) -> Net-(R22-Pad2)
- U3 pad 2: Net-(R18-Pad1) -> Net-(D10-K)
- U3 pad 3: VDD -> /IN_1_2
- U3 pad 4: /b1 -> VDD
- U4 pad 1: Net-(J3-io-Pad6) -> Net-(R23-Pad2)
- U4 pad 2: Net-(R19-Pad1) -> Net-(D11-K)
- U4 pad 3: VDD -> /IN_1_3
- U4 pad 4: /b2 -> VDD
- U5 pad 1: Net-(J3-io-Pad8) -> Net-(R24-Pad2)
- U5 pad 2: Net-(R20-Pad1) -> Net-(D12-K)
- U5 pad 3: VDD -> /IN_1_4
- U5 pad 4: /b3 -> VDD
- U6 pad 1: Net-(J4-io-Pad2) -> Net-(R25-Pad2)
- U6 pad 2: Net-(R21-Pad1) -> Net-(D13-K)
- U6 pad 3: VDD -> /IN_1_5
- U6 pad 4: /b4 -> VDD
- U7 pad 1: Net-(J4-io-Pad4) -> Net-(R26-Pad2)
- U7 pad 2: Net-(R22-Pad1) -> Net-(D14-K)
- U7 pad 3: VDD -> /IN_1_6
- U7 pad 4: /b5 -> VDD
- U8 pad 1: Net-(J4-io-Pad6) -> Net-(R27-Pad2)
- U8 pad 2: Net-(R23-Pad1) -> Net-(D15-K)
- U8 pad 3: VDD -> /IN_1_7
- U8 pad 4: /b6 -> VDD
- U9 pad 1: Net-(J4-io-Pad8) -> Net-(R28-Pad2)
- U9 pad 2: Net-(R24-Pad1) -> Net-(D16-K)
- U9 pad 3: VDD -> /IN_1_8
- U9 pad 4: /b7 -> VDD
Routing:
- net VDD: track 259.8 -> 0.00 mm, vias 1 -> 0
- net /b6: track 133.0 -> 0.00 mm, vias 5 -> 0
- net /b7: track 124.2 -> 0.00 mm, vias 1 -> 0
- net /a7: track 105.1 -> 0.00 mm, vias 3 -> 0
- net /b4: track 97.3 -> 0.00 mm, vias 3 -> 0
- net /b5: track 95.4 -> 0.00 mm
- net /b3: track 94.0 -> 0.00 mm, vias 3 -> 0
- net /b2: track 91.5 -> 0.00 mm, vias 3 -> 0
- net /b1: track 88.9 -> 0.00 mm, vias 3 -> 0
- net /b0: track 86.0 -> 0.00 mm, vias 3 -> 0
- net /a6: track 78.3 -> 0.00 mm
- net /a5: track 73.5 -> 0.00 mm, vias 1 -> 0
- net /a4: track 68.5 -> 0.00 mm, vias 2 -> 0
- net GND: track 66.7 -> 0.00 mm
- net /a3: track 63.4 -> 0.00 mm, vias 2 -> 0
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- removed copper zone on B.Cu, net GND
- removed copper zone on F.Cu, net GND
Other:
- board size 124.5 x 95.9 mm -> 124.5 x 174.6 mm
- board text removed: "1 0"
- board text removed: "A1"
- board text removed: "A2"
- board text removed: "ADR A0 A1 A2 0 0 0 0 1 1 0 0 2 0 1 0 3 1 1 0 4 0 0 1 5 1 0 1 6 0 1 1 7 1 1 1"
